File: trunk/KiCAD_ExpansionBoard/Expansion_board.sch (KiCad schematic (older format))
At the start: 36 parts, among them P1 ANT_GND, P5 ANT_C, Q1 NTR4101P, Q3 PDTC124XT, SW1 SLIDE_SWITCH_SPDT, SW2 SLIDE_SWITCH_4PDT, U1 SN65HVD234, U2 TPS62160, U3 SN65HVD11, U4 RFM23B

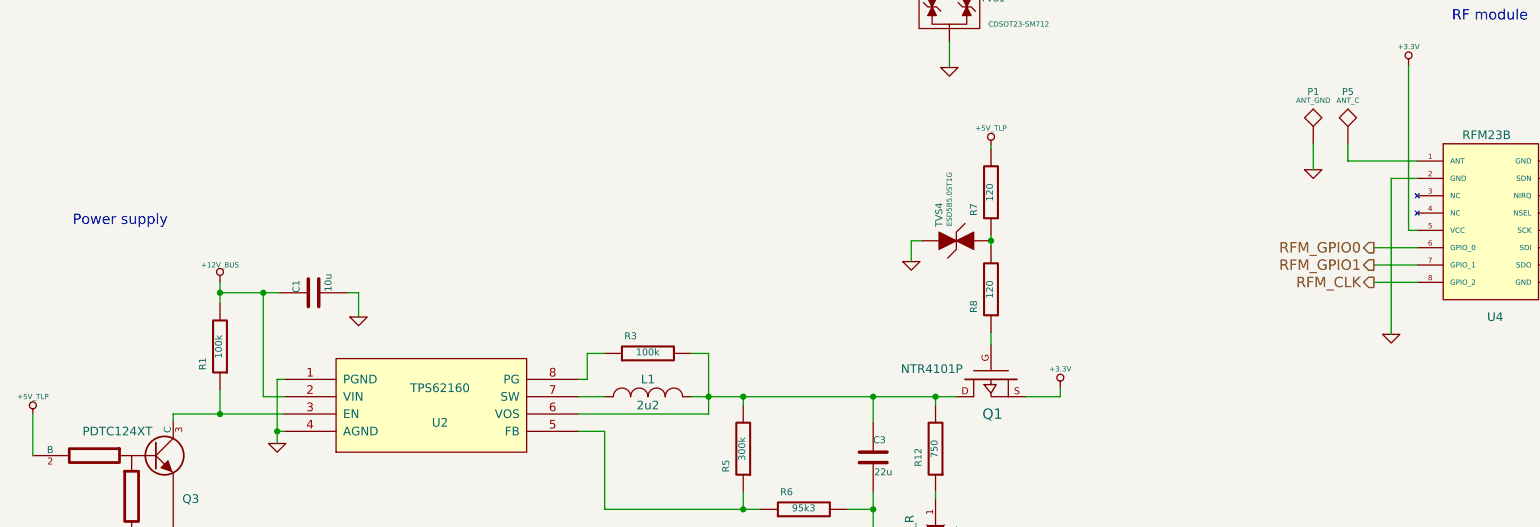
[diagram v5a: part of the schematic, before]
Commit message: Eliminata R8 e collegata la piazzola P1 direttamente al pin 2 del RFM23B. Schema elettrico alla versione 0.3.3 Cretata la BOM definitiva in (TM4C123G_CommExpBoard_BOM.xlsx e TM4C123G_CommExpBoard.csv) Completato lo sbroglio del PCB con serigrafie posizionate complete di logo OHSW. PCB alla versione 0.2
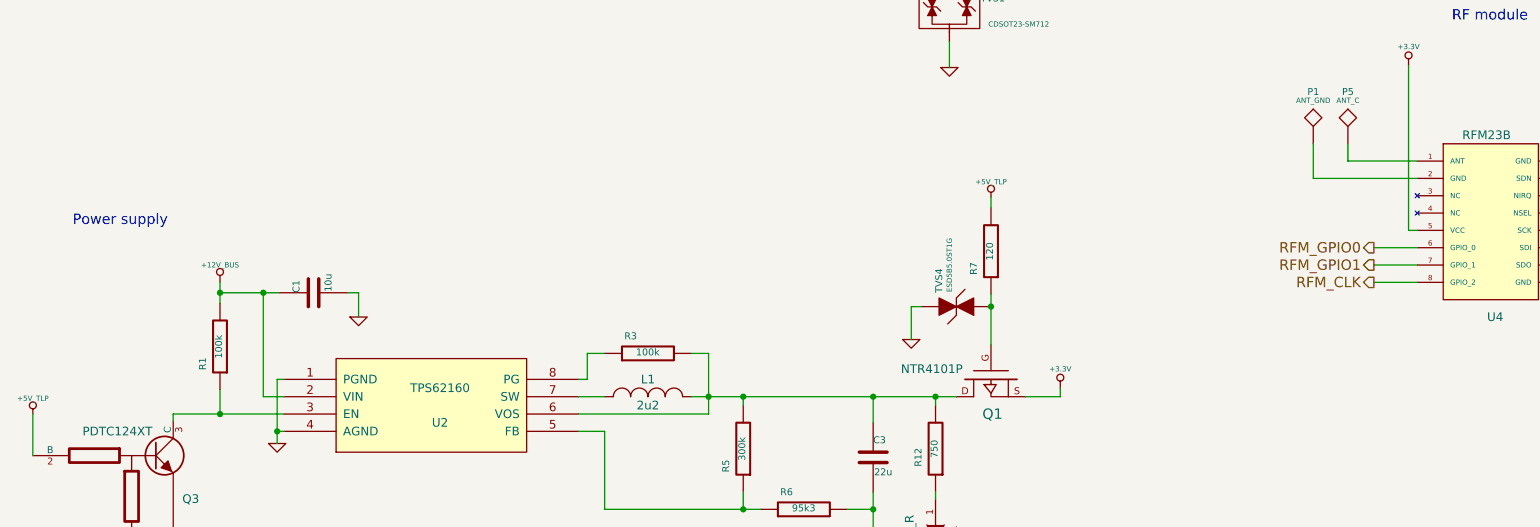
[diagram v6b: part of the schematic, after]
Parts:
- removed R8: 120, ~, symbol R
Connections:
- net GND: no longer P1.1, U4.2 (GND)
- net at Q1.G: now also R7.1, TVS4.2
- new net: P1.1, U4.2 (GND)
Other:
- moved on the sheet: R7, TVS4

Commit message: Schema elettrico: variate le connessione del partitore di fail-safe-biasing. R13 è di pull-down ed R15 di pull-up, quindi sono connesse rispettivamente verso gnd e +3.3V. In precedenza erano scambiate. PCB: variato il layout seguendo ciò che è stato fatto per lo schema elettrico. Risistemata la zona di rame sotto a L1 poichè in seguito alla modifica precedente, ha dato problemi (credo dovuti al cambio nome della pista).
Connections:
- net +3.3V: now also R15.1; no longer R13.1
- net GND: now also R13.1; no longer R15.1
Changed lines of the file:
@@
 Sheet 2 3
 Title "TM4C123G Communication Expansion Board"
-Date "6 aug 2014"
-Rev "0.3.4"
+Date "7 aug 2014"
+Rev "0.3.5"
 Comp "Luca Buccolini, Student @ Università Politecnica delle Marche"
 Comment1 "Expansion Board for the Texas Instruments TM4C123G Launchpad "
@@
 $EndComp
 $Comp
-L GND #PWR04
-U 1 1 5398D44B
-P 9290 2960
-F 0 "#PWR04" H 9290 2960 30  0001 C CNN
-F 1 "GND" H 9290 2890 30  0001 C CNN
-F 2 "" H 9290 2960 60  0000 C CNN
-F 3 "" H 9290 2960 60  0000 C CNN
-	1    9290 2960
-	1    0    0    -1
-$EndComp
-$Comp
 L INDUCTOR_SMALL L1
 U 1 1 5398D684
@@
 $EndComp
 $Comp
-L GND #PWR05
+L GND #PWR04
 U 1 1 5398E022
 P 5600 7450
-F 0 "#PWR05" H 5600 7450 30  0001 C CNN
+F 0 "#PWR04" H 5600 7450 30  0001 C CNN
 F 1 "GND" H 5600 7380 30  0001 C CNN
 F 2 "" H 5600 7450 60  0000 C CNN
@@
 $EndComp
 $Comp
-L GND #PWR06
+L GND #PWR05
 U 1 1 5399DA32
 P 1440 4020
-F 0 "#PWR06" H 1440 4020 30  0001 C CNN
+F 0 "#PWR05" H 1440 4020 30  0001 C CNN
 F 1 "GND" H 1440 3950 30  0001 C CNN
 F 2 "" H 1440 4020 60  0000 C CNN
@@
 $EndComp
 $Comp
-L GND #PWR07
+L GND #PWR06
 U 1 1 5399DD28
 P 2240 3270
-F 0 "#PWR07" H 2240 3270 30  0001 C CNN
+F 0 "#PWR06" H 2240 3270 30  0001 C CNN
 F 1 "GND" H 2240 3200 30  0001 C CNN
 F 2 "" H 2240 3270 60  0000 C CNN
@@
 CAN0_TX
 $Comp
-L GND #PWR08
+L GND #PWR07
 U 1 1 539A0CDF
 P 6040 4520
-F 0 "#PWR08" H 6040 4520 30  0001 C CNN
+F 0 "#PWR07" H 6040 4520 30  0001 C CNN
 F 1 "GND" H 6040 4450 30  0001 C CNN
 F 2 "" H 6040 4520 60  0000 C CNN
@@
 RF module
 $Comp
-L GND #PWR09
+L GND #PWR08
 U 1 1 53A2EC9E
 P 9690 6060
-F 0 "#PWR09" H 9690 6060 30  0001 C CNN
+F 0 "#PWR08" H 9690 6060 30  0001 C CNN
 F 1 "GND" H 9690 5990 30  0001 C CNN
 F 2 "" H 9690 6060 60  0000 C CNN
@@
 $EndComp
 $Comp
-L GND #PWR010
+L GND #PWR09
 U 1 1 53A2ED44
 P 850 910
-F 0 "#PWR010" H 850 910 30  0001 C CNN
+F 0 "#PWR09" H 850 910 30  0001 C CNN
 F 1 "GND" H 850 840 30  0001 C CNN
 F 2 "" H 850 910 60  0000 C CNN
@@
 $EndComp
 $Comp
-L PWR_FLAG #FLG011
+L PWR_FLAG #FLG010
 U 1 1 53A2ED4C
 P 850 810
-F 0 "#FLG011" H 850 905 30  0001 C CNN
+F 0 "#FLG010" H 850 905 30  0001 C CNN
 F 1 "PWR_FLAG" H 850 990 30  0000 C CNN
 F 2 "~" H 850 810 60  0000 C CNN
@@
 NoConn ~ 8690 2410
 $Comp
+L +3.3V #PWR011
+U 1 1 53B3C601
+P 9240 2770
+F 0 "#PWR011" H 9240 2730 30  0001 C CNN
+F 1 "+3.3V" H 9240 2880 30  0000 C CNN
+F 2 "~" H 9240 2770 60  0000 C CNN
+F 3 "~" H 9240 2770 60  0000 C CNN
+	1    9240 2770
+	1    0    0    -1
+$EndComp
+$Comp
 L +3.3V #PWR012
-U 1 1 53B3C601
-P 9560 710
-F 0 "#PWR012" H 9560 670 30  0001 C CNN
-F 1 "+3.3V" H 9560 820 30  0000 C CNN
-F 2 "~" H 9560 710 60  0000 C CNN
-F 3 "~" H 9560 710 60  0000 C CNN
-	1    9560 710
-	1    0    0    -1
-$EndComp
-$Comp
-L +3.3V #PWR013
 U 1 1 53B3C60E
 P 8040 910
-F 0 "#PWR013" H 8040 870 30  0001 C CNN
+F 0 "#PWR012" H 8040 870 30  0001 C CNN
 F 1 "+3.3V" H 8040 1020 30  0000 C CNN
 F 2 "~" H 8040 910 60  0000 C CNN
@@
 $EndComp
 $Comp
-L +3.3V #PWR014
+L +3.3V #PWR013
 U 1 1 53B3C614
 P 1640 2970
-F 0 "#PWR014" H 1640 2930 30  0001 C CNN
+F 0 "#PWR013" H 1640 2930 30  0001 C CNN
 F 1 "+3.3V" H 1640 3080 30  0000 C CNN
 F 2 "~" H 1640 2970 60  0000 C CNN
@@
 $EndComp
 $Comp
-L +3.3V #PWR015
+L +3.3V #PWR014
 U 1 1 53B3C61A
 P 8690 4510
-F 0 "#PWR015" H 8690 4470 30  0001 C CNN
+F 0 "#PWR014" H 8690 4470 30  0001 C CNN
 F 1 "+3.3V" H 8690 4620 30  0000 C CNN
 F 2 "~" H 8690 4510 60  0000 C CNN
@@
 $EndComp
 $Comp
-L +3.3V #PWR016
+L +3.3V #PWR015
 U 1 1 53B3C62A
 P 9890 4510
-F 0 "#PWR016" H 9890 4470 30  0001 C CNN
+F 0 "#PWR015" H 9890 4470 30  0001 C CNN
 F 1 "+3.3V" H 9890 4620 30  0000 C CNN
 F 2 "~" H 9890 4510 60  0000 C CNN
@@
 $EndComp
 $Comp
-L +3.3V #PWR017
+L +3.3V #PWR016
 U 1 1 53B3C636
 P 6680 6370
-F 0 "#PWR017" H 6680 6330 30  0001 C CNN
+F 0 "#PWR016" H 6680 6330 30  0001 C CNN
 F 1 "+3.3V" H 6680 6480 30  0000 C CNN
 F 2 "~" H 6680 6370 60  0000 C CNN
@@
 $EndComp
 $Comp
-L GND #PWR018
+L GND #PWR017
 U 1 1 53B42358
 P 2160 6690
-F 0 "#PWR018" H 2160 6690 30  0001 C CNN
+F 0 "#PWR017" H 2160 6690 30  0001 C CNN
 F 1 "GND" H 2160 6620 30  0001 C CNN
 F 2 "~" H 2160 6690 60  0000 C CNN
@@
 $EndComp
 $Comp
-L GND #PWR019
+L GND #PWR018
 U 1 1 53B4247C
 P 2630 5960
-F 0 "#PWR019" H 2630 5960 30  0001 C CNN
+F 0 "#PWR018" H 2630 5960 30  0001 C CNN
 F 1 "GND" H 2630 5890 30  0001 C CNN
 F 2 "~" H 2630 5960 60  0000 C CNN
@@
 $EndComp
 $Comp
-L +12V_BUS #PWR020
+L +12V_BUS #PWR019
 U 1 1 53B42548
 P 1830 5760
-F 0 "#PWR020" H 1830 5710 20  0001 C CNN
+F 0 "#PWR019" H 1830 5710 20  0001 C CNN
 F 1 "+12V_BUS" H 1830 5860 30  0000 C CNN
 F 2 "~" H 1830 5760 60  0000 C CNN
@@
 $EndComp
 $Comp
-L GND #PWR021
+L GND #PWR020
 U 1 1 53B42799
 P 1560 7360
-F 0 "#PWR021" H 1560 7360 30  0001 C CNN
+F 0 "#PWR020" H 1560 7360 30  0001 C CNN
 F 1 "GND" H 1560 7290 30  0001 C CNN
 F 2 "~" H 1560 7360 60  0000 C CNN
@@
 $EndComp
 $Comp
-L GND #PWR022
+L GND #PWR021
 U 1 1 53B43870
 P 5960 7450
-F 0 "#PWR022" H 5960 7450 30  0001 C CNN
+F 0 "#PWR021" H 5960 7450 30  0001 C CNN
 F 1 "GND" H 5960 7380 30  0001 C CNN
 F 2 "" H 5960 7450 60  0000 C CNN
@@
 	5440 1560 6240 1560
 Wire Wire Line
-	9240 2860 9290 2860
-Wire Wire Line
-	9560 760  9560 710
-Wire Wire Line
 	4850 6970 4850 7070
 Wire Wire Line
@@
 	8890 1710 8890 1760
 Wire Wire Line
-	9290 2860 9290 2960
-Wire Wire Line
 	8740 2760 8740 2860
 Wire Wire Line
@@
 Connection ~ 8790 2310
 $Comp
-L GND #PWR023
+L GND #PWR022
 U 1 1 53BFC020
 P 5820 6090
-F 0 "#PWR023" H 5820 6090 30  0001 C CNN
+F 0 "#PWR022" H 5820 6090 30  0001 C CNN
 F 1 "GND" H 5820 6020 30  0001 C CNN
 F 2 "" H 5820 6090 60  0000 C CNN
@@
 Connection ~ 6280 5900
 $Comp
-L +5V_TLP #PWR024
+L +5V_TLP #PWR023
 U 1 1 53D82DB4
 P 750 6520
-F 0 "#PWR024" H 750 6610 20  0001 C CNN
+F 0 "#PWR023" H 750 6610 20  0001 C CNN
 F 1 "+5V_TLP" H 750 6610 30  0000 C CNN
 F 2 "~" H 750 6520 60  0000 C CNN
@@
 $EndComp
 $Comp
-L +5V_TLP #PWR025
+L +5V_TLP #PWR024
 U 1 1 53D82F93
 P 6280 5270
-F 0 "#PWR025" H 6280 5360 20  0001 C CNN
+F 0 "#PWR024" H 6280 5360 20  0001 C CNN
 F 1 "+5V_TLP" H 6280 5360 30  0000 C CNN
 F 2 "~" H 6280 5270 60  0000 C CNN
@@
 	1    0    0    -1
 $EndComp
+$Comp
+L GND #PWR025
+U 1 1 5398D44B
+P 9560 940
+F 0 "#PWR025" H 9560 940 30  0001 C CNN
+F 1 "GND" H 9560 870 30  0001 C CNN
+F 2 "" H 9560 940 60  0000 C CNN
+F 3 "" H 9560 940 60  0000 C CNN
+	1    9560 940
+	1    0    0    -1
+$EndComp
+Wire Wire Line
+	9560 940  9560 760
+Wire Wire Line
+	9240 2770 9240 2860
 $EndSCHEMATC
